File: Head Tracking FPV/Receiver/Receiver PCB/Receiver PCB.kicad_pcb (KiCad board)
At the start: 2 copper layers, 57 x 59.5 mm, 7 parts, among them J1 Conn_01x02_Pin, J2 Pan Servo, J3 Tilt Servo, J4 Conn_01x05_Pin, J5 VTX Power, SW1 SW_SPDT, U1 ESP32-DEVKIT-V1

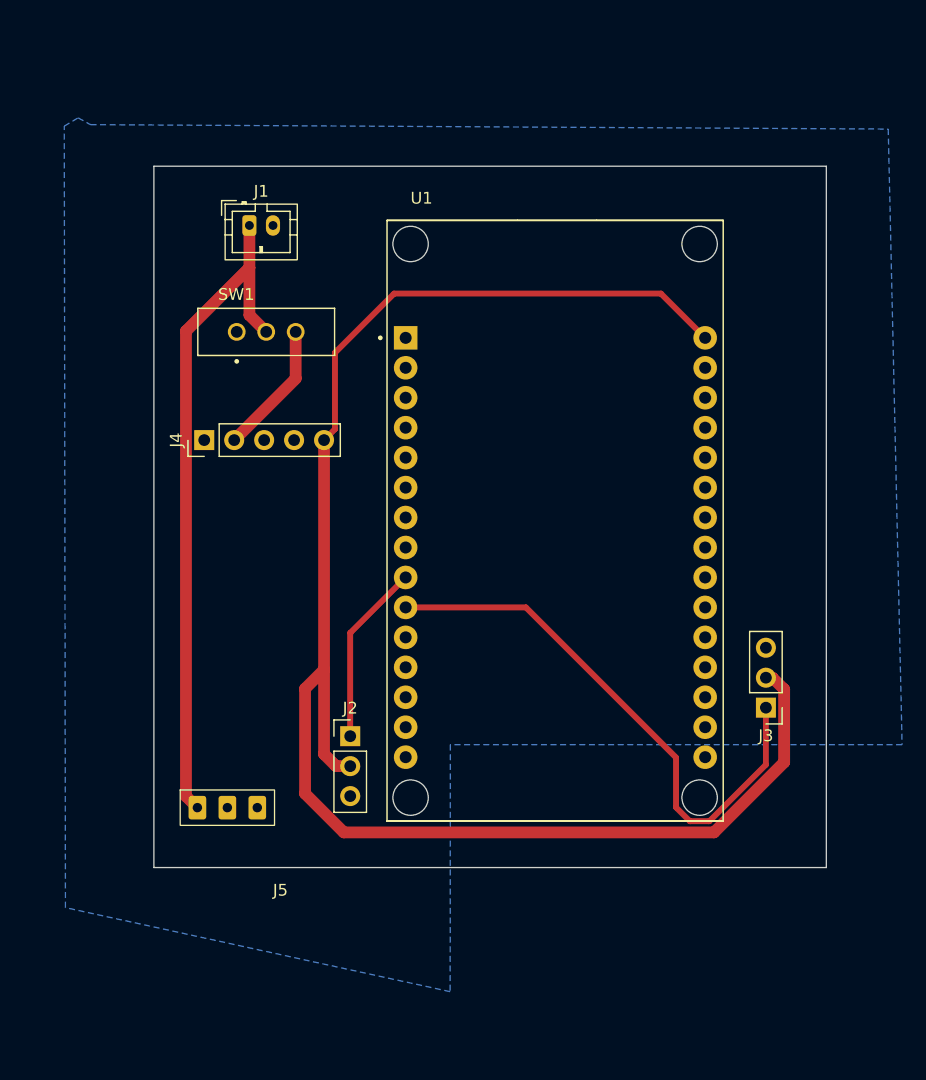
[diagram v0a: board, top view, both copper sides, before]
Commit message: Added Mounting Holes
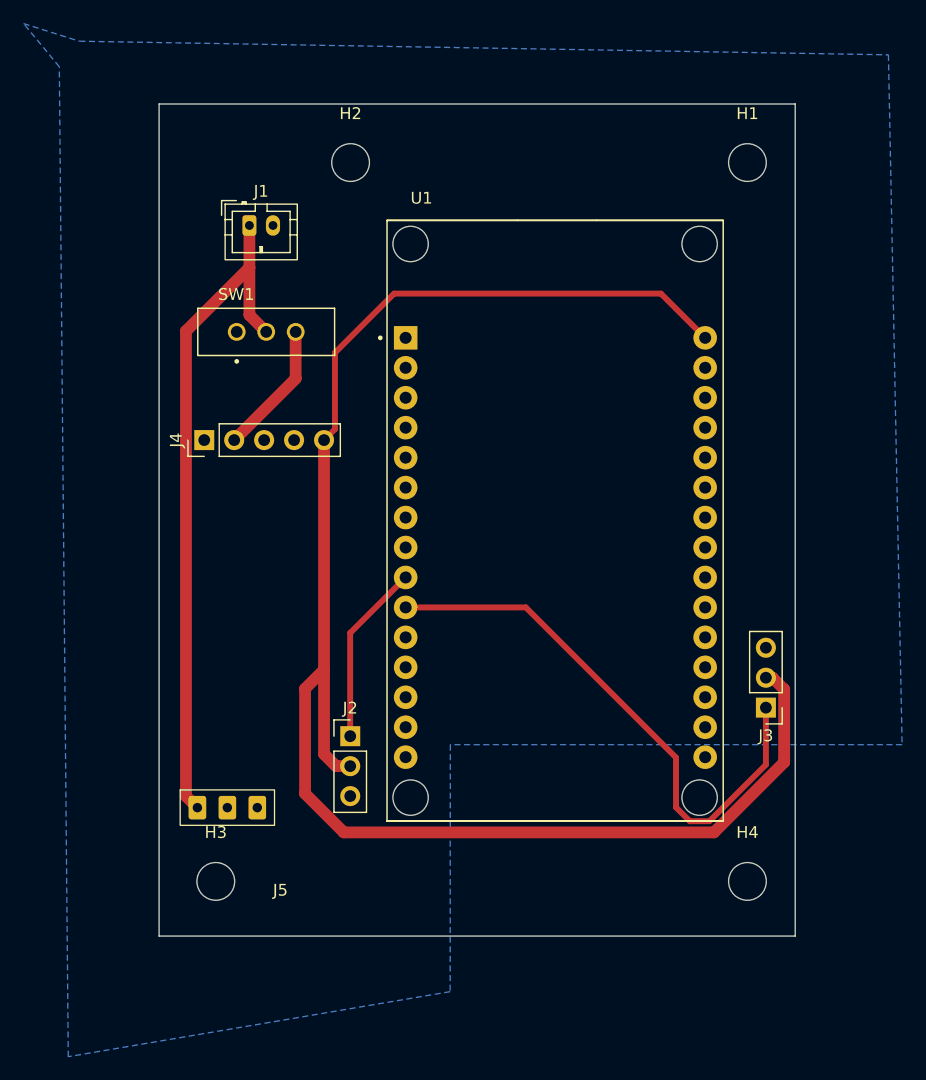
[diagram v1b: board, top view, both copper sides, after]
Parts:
- added H1: MountingHole, MountingHole:MountingHole_3.2mm_M3, F.Cu at (146.7, 69.2)
- added H2: MountingHole, MountingHole:MountingHole_3.2mm_M3, F.Cu at (113.0, 69.2)
- added H3: MountingHole, MountingHole:MountingHole_3.2mm_M3, F.Cu at (101.6, 130.2)
- added H4: MountingHole, MountingHole:MountingHole_3.2mm_M3, F.Cu at (146.7, 130.2)
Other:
- board size 57 x 59.5 mm -> 53.9 x 70.6 mm
